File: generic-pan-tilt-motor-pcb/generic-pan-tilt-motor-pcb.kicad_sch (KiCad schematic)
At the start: 35 parts, among them J1 B12B-PH-SM4-TBT, J2 S4B-PH-SM4-TB, J3 S4B-PH-SM4-TB, J4 1945096, J5 1945119, J6 1945151

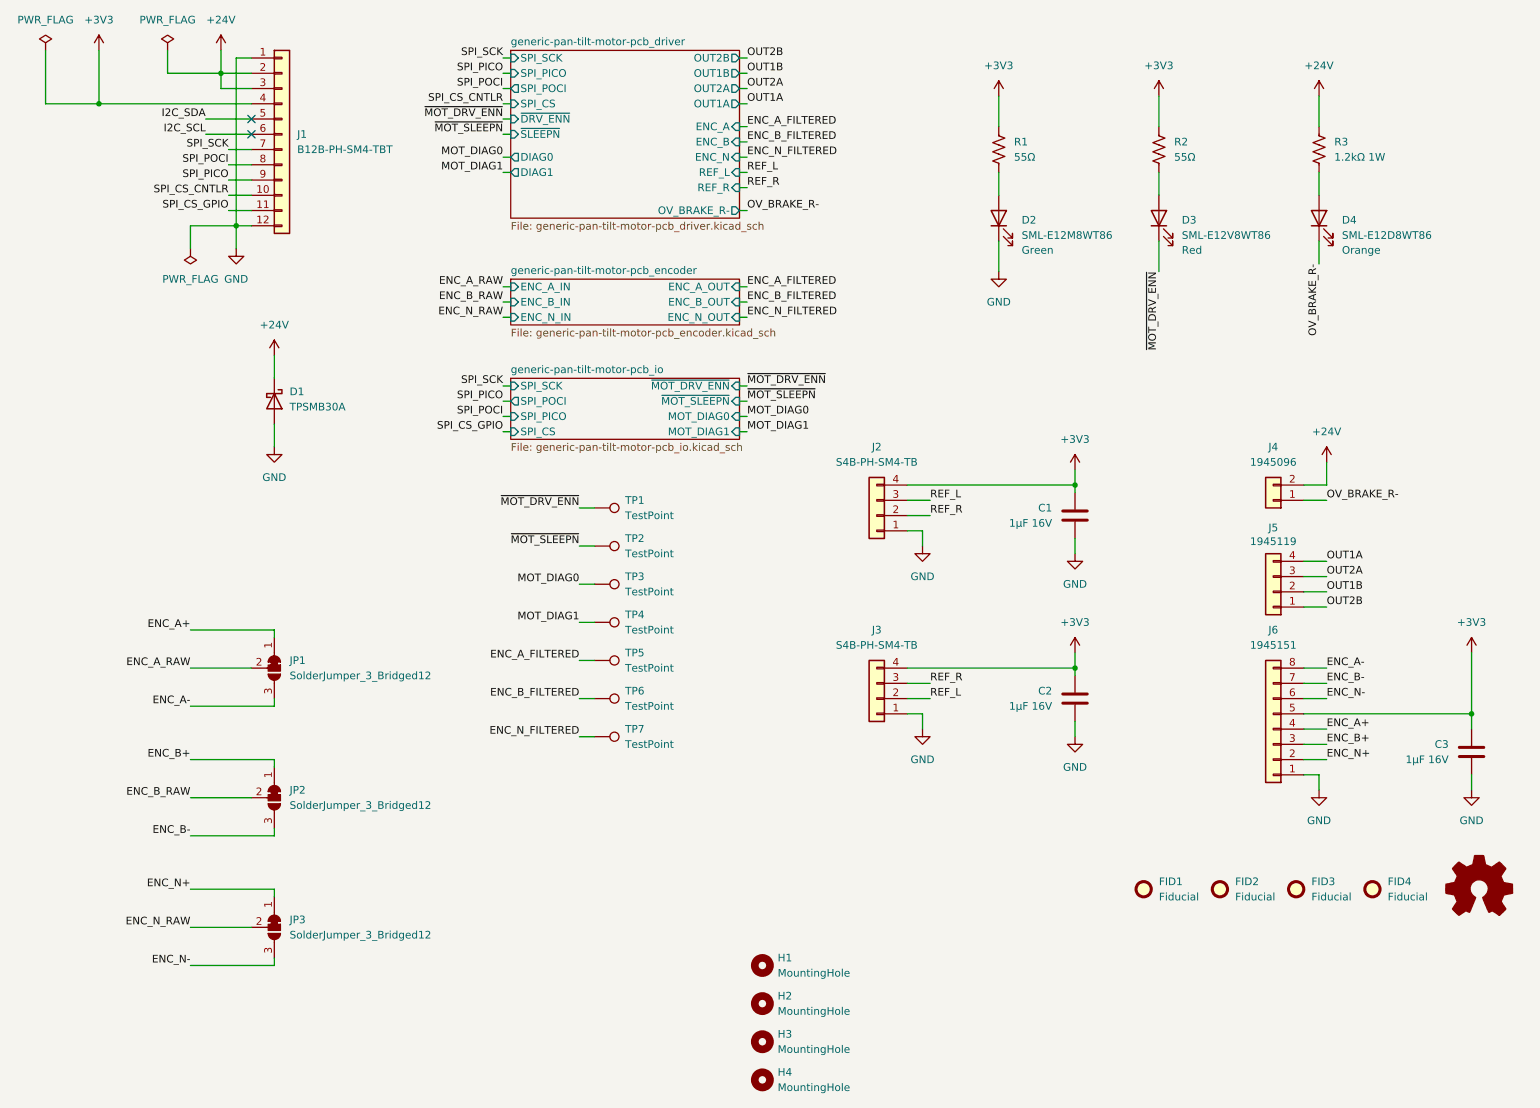
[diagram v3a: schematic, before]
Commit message: fix part numbers, add newark parts, separate fields for part desc
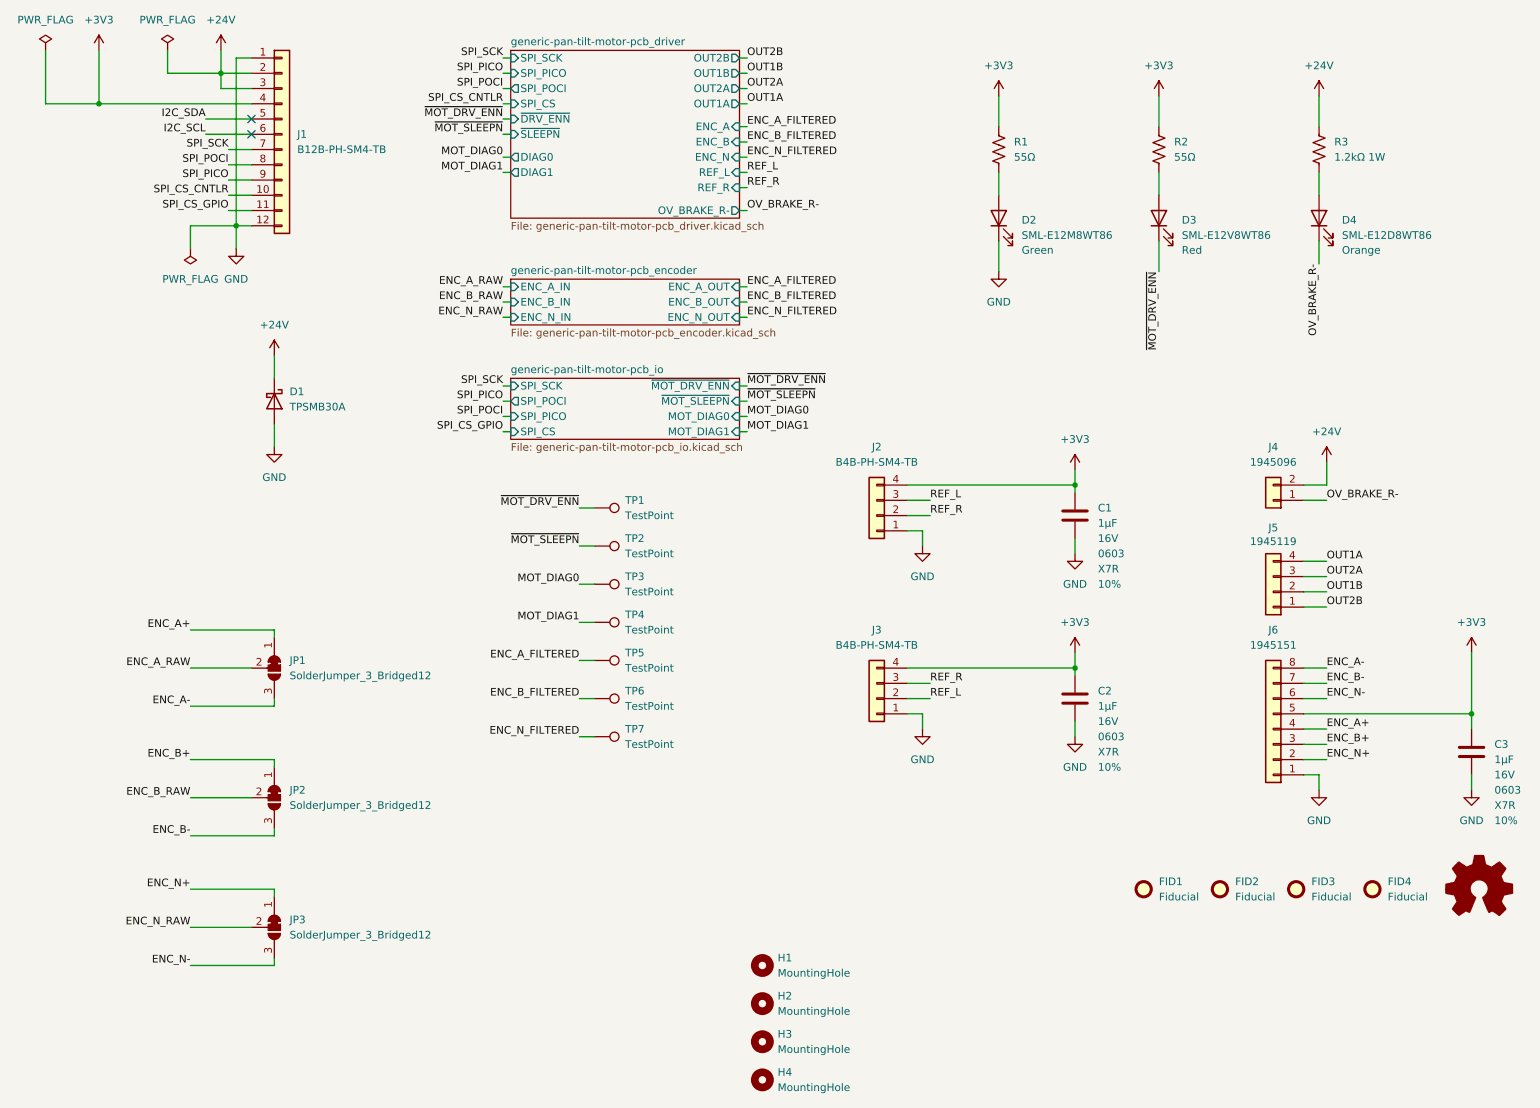
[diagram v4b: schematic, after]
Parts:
- C1, C2, C3: value 1µF 16V -> 1µF; Case Code (none) -> 0603; Dielectric (none) -> X7R; Tolerance (none) -> 10%; Voltage (none) -> 16V; manf# (none) -> CL10B104KO8NFNC; mouser# (none) -> 187-­CL10B104KO8NFNC
- D1: newark# (none) -> 67AH3299
- D2: newark# (none) -> 18AC7715
- D3: newark# (none) -> 18AC7719
- D4: newark# (none) -> 18AC7714
- J1: value B12B-PH-SM4-TBT -> B12B-PH-SM4-TB; digikey# 455-S12B-PH-SM4-TBCT-ND -> 455-B12B-PH-SM4-TBCT-ND; manf# S12B-PH-SM4-TB -> B12B-PH-SM4-TB; newark# (none) -> 90R9305
- J2, J3: value S4B-PH-SM4-TB -> B4B-PH-SM4-TB; digikey# 455-S4B-PH-SM4-TBCT-ND -> 455-B4B-PH-SM4-TBCT-ND; manf# S4B-PH-SM4-TB -> B4B-PH-SM4-TB; newark# (none) -> 37K9959
- J4: digikey# 277-1749-ND -> 277-1749-ND|277-1706-ND; manf# 1945096 -> 1945096|1984015; mouser# 651-1945096 -> 651-1945096|651-1984015; newark# (none) -> 69R9968|70R0001
- J5: digikey# 277-1751-ND -> 277-1751-ND|277-1708-ND; manf# 1945119 -> 1945119|1984031; mouser# 651-1945119 -> 651-1945119|651-1984031; newark# (none) -> 69R9970|70R0007
- J6: digikey# 277-1755-ND -> 277-1755-ND|277-1709-ND; manf# 1945151 -> 1945151|1984044; mouser# 651-1945151 -> 651-1945151|651-1984044; newark# (none) -> 69R9974|

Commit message: motor fix flipped spi mcp, spi tristate for drc, silk screw terminals, all parts manf and vendors
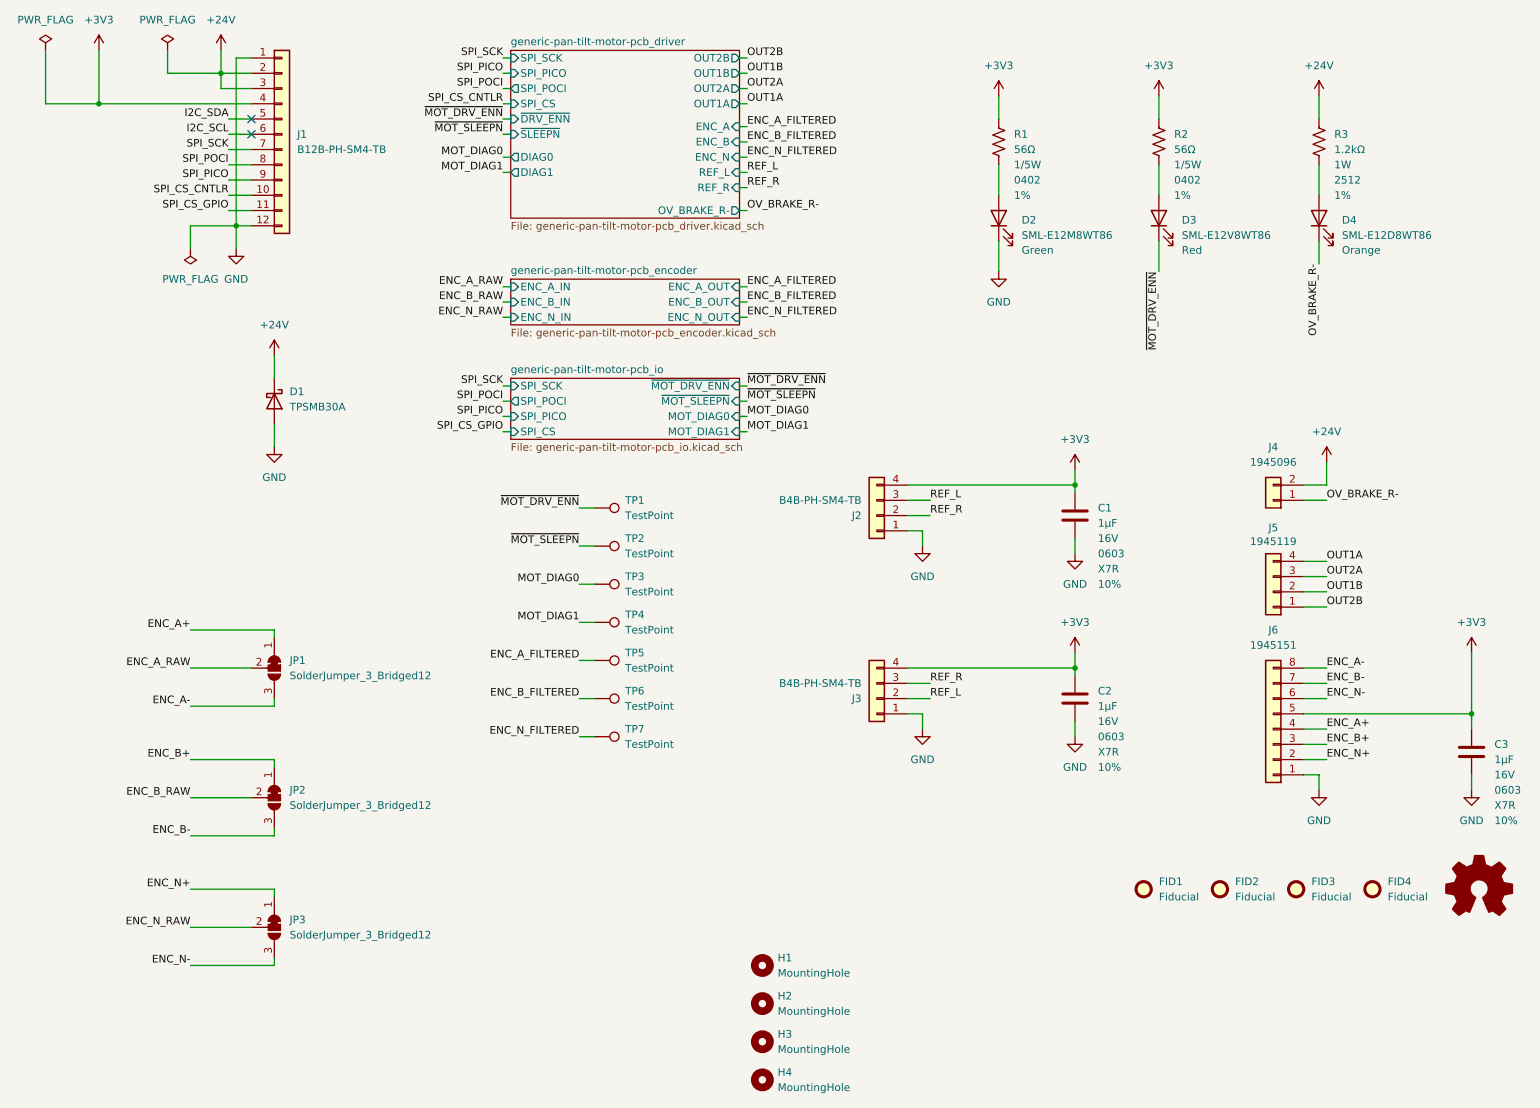
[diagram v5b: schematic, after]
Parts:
- C1, C2, C3: digikey# (none) -> 1276-1005-1-ND; lcsc# (none) -> C66501; manf# CL10B104KO8NFNC -> CL10B104KO8NNNC; mouser# 187-­CL10B104KO8NFNC -> 187-­CL10B104KO8NNNC; newark# (none) -> 82AC9325
- D1: lcsc# (none) -> C428851
- D2: lcsc# (none) -> C2837819
- D3: lcsc# (none) -> C510294
- D4: lcsc# (none) -> C5336488
- J1: lcsc# (none) -> C545752
- J2, J3: goldphoenix# (none) -> 122-B4B-PH-SM4-TB(LF)(SN)-CT; lcsc# (none) -> C160354
- J4: goldphoenix# (none) -> 139-1945096-CT|139-1984015-CT; lcsc# (none) -> C5266024|C3580047
- J5: goldphoenix# (none) -> 139-1945119-CT|139-1984031-CT; lcsc# (none) -> C5266029|C5443578
- J6: digikey# 277-1755-ND|277-1709-ND -> 277-1755-ND|277-1712-ND; goldphoenix# (none) -> 139-1945151-CT; lcsc# (none) -> |C21692588; manf# 1945151|1984044 -> 1945151|1984073; mouser# 651-1945151|651-1984044 -> 651-1945151|651-1984073; newark# 69R9974| -> 69R9974|70R0016
- R1, R2: value 55Ω -> 56Ω; Case Code (none) -> 0402; Power (none) -> 1/5W; Tolerance (none) -> 1%; digikey# (none) -> 541-10417-1-ND; lcsc# (none) -> C4063621; manf# (none) -> RCS040256R0FKED; mouser# (none) -> 71-RCS040256R0FKED
- R3: value 1.2kΩ 1W -> 1.2kΩ; Case Code (none) -> 2512; Power (none) -> 1W; Tolerance (none) -> 1%; digikey# (none) -> RMCF2512FT1K20CT-ND; lcsc# (none) -> C3943439; manf# (none) -> RMCF2512FT1K20; mouser# (none) -> 708-RMCF2512FT1K20
- TP1, TP2, TP3, TP4, TP5, TP6, TP7: now left out of the parts list
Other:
- moved on the sheet: R2, R3

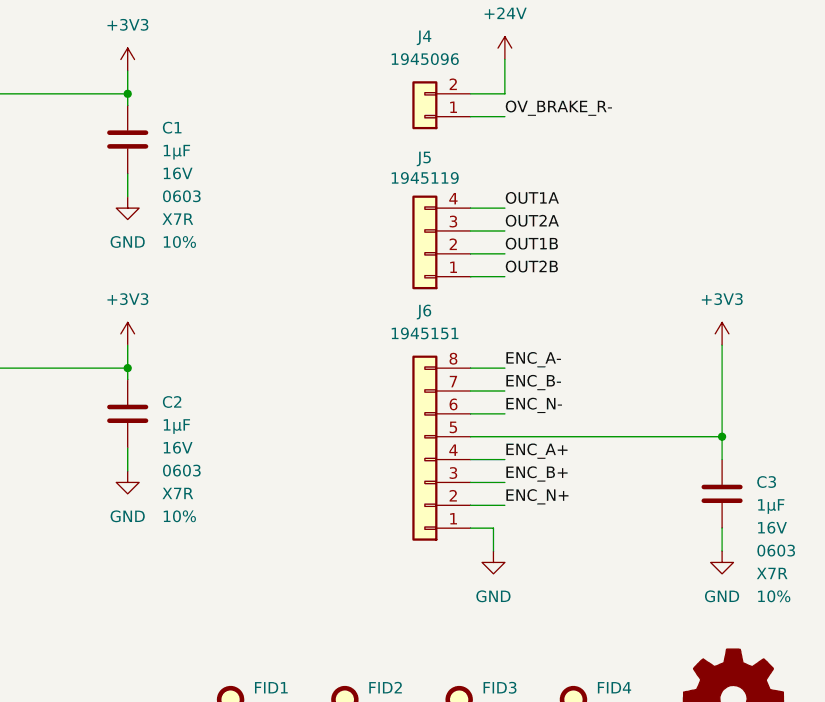
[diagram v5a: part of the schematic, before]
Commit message: motor fix incorrect cap part
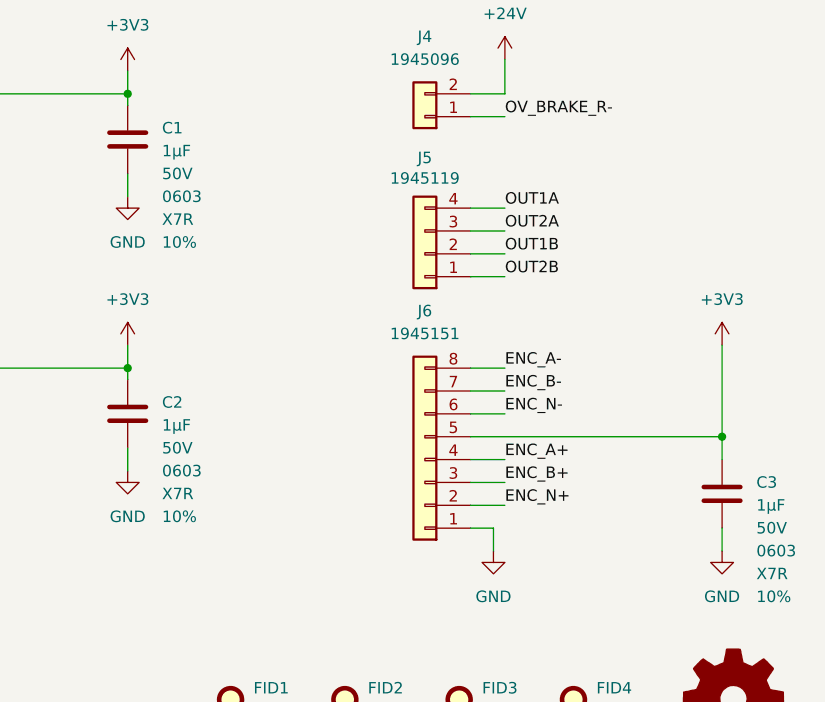
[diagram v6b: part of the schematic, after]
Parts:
- C1, C2, C3: Voltage 16V -> 50V; digikey# 1276-1005-1-ND -> (none); lcsc# C66501 -> C5199872; manf# CL10B104KO8NNNC -> CL10B105KB8NQNC; mouser# 187-­CL10B104KO8NNNC -> 187­-CL10B105KB8NQNC; newark# 82AC9325 -> (none)
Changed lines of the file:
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@@
 			)
 		)
-		(property "Voltage" "16V"
+		(property "Voltage" "50V"
 			(at 195.58 106.6799 0)
 			(effects
@@
 			)
 		)
-		(property "manf#" "CL10B104KO8NNNC"
+		(property "manf#" "CL10B105KB8NQNC"
 			(at 191.77 102.87 0)
 			(effects
@@
 			)
 		)
-		(property "mouser#" "187-­CL10B104KO8NNNC"
+		(property "mouser#" "187­-CL10B105KB8NQNC"
 			(at 191.77 102.87 0)
 			(effects
@@
 			)
 		)
-		(property "digikey#" "1276-1005-1-ND"
-			(at 191.77 102.87 0)
-			(effects
-				(font
-					(size 1.27 1.27)
-				)
-				(hide yes)
-			)
-		)
-		(property "lcsc#" "C66501"
-			(at 191.77 102.87 0)
-			(effects
-				(font
-					(size 1.27 1.27)
-				)
-				(hide yes)
-			)
-		)
-		(property "newark#" "82AC9325"
+		(property "lcsc#" "C5199872"
 			(at 191.77 102.87 0)
 			(effects
@@
 			)
 		)
-		(property "Voltage" "16V"
+		(property "Voltage" "50V"
 			(at 195.58 137.1599 0)
 			(effects
@@
 			)
 		)
-		(property "manf#" "CL10B104KO8NNNC"
-			(at 191.77 133.35 0)
-			(effects
-				(font
-					(size 1.27 1.27)
-				)
-				(hide yes)
-			)
-		)
-		(property "mouser#" "187-­CL10B104KO8NNNC"
+		(property "manf#" "CL10B105KB8NQNC"
 			(at 191.77 133.35 0)
 			(effects
@@
 			)
 		)
-		(property "digikey#" "1276-1005-1-ND"
+		(property "mouser#" "187­-CL10B105KB8NQNC"
 			(at 191.77 133.35 0)
 			(effects
@@
 			)
 		)
-		(property "lcsc#" "C66501"
-			(at 191.77 133.35 0)
-			(effects
-				(font
-					(size 1.27 1.27)
-				)
-				(hide yes)
-			)
-		)
-		(property "newark#" "82AC9325"
+		(property "lcsc#" "C5199872"
 			(at 191.77 133.35 0)
 			(effects
@@
 			)
 		)
-		(property "Voltage" "16V"
+		(property "Voltage" "50V"
 			(at 261.62 146.0499 0)
 			(effects
@@
 			)
 		)
-		(property "manf#" "CL10B104KO8NNNC"
-			(at 257.81 142.24 0)
-			(effects
-				(font
-					(size 1.27 1.27)
-				)
-				(hide yes)
-			)
-		)
-		(property "mouser#" "187-­CL10B104KO8NNNC"
-			(at 257.81 142.24 0)
-			(effects
-				(font
-					(size 1.27 1.27)
-				)
-				(hide yes)
-			)
-		)
-		(property "digikey#" "1276-1005-1-ND"
+		(property "manf#" "CL10B105KB8NQNC"
 			(at 257.81 142.24 0)
 			(effects
@@
 			)
 		)
-		(property "lcsc#" "C66501"
+		(property "mouser#" "187­-CL10B105KB8NQNC"
 			(at 257.81 142.24 0)
 			(effects
@@
 			)
 		)
-		(property "newark#" "82AC9325"
+		(property "lcsc#" "C5199872"
 			(at 257.81 142.24 0)
 			(effects
